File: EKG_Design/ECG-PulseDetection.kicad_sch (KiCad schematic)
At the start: 0 parts

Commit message: Started EKG-Details and ECG-PulseDetection Circuit Symbols implemented
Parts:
- added C11: C_Small, symbol Device:C_Small
- added D1, D2: BAR43FILM, Package_TO_SOT_SMD:SOT-23, symbol Diode:BAR43FILM
- added D3: LED, symbol Device:LED
- added Q1: BC848, Package_TO_SOT_SMD:SOT-23, symbol Transistor_BJT:BC848
- added R3, R4: R, symbol Device:R
- added RV1, RV2: R_Potentiometer, symbol Device:R_Potentiometer
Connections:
- new net: D3.2 (A), R4.2
- new net: C11.1, D2.3 (K), R3.1, RV2.2, RV2.3
- new net: D1.3 (K), D2.1 (A), RV1.2
- new net: Q1.1 (B), R3.2
- new net: D3.1 (K), Q1.3 (C)
- new net 5V0_Analog: R4.1
- new net ECG_Out: RV1.1
- new net GNDD: C11.2, Q1.2 (E), RV1.3, RV2.1
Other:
- company: (none) -> HAWK
- title: (none) -> EKG-Verstärker

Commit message: Finished EKG Schematic
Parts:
- removed D1, D2: BAR43FILM, Package_TO_SOT_SMD:SOT-23, symbol Diode:BAR43FILM
- added D103: BAR43SFILM, Package_TO_SOT_SMD:SOT-23, symbol CustomSymbols:BAR43SFILM
- C301: renamed from C11; value C_Small -> 10u/6.3V X5R
- D303: renamed from D3; value LED -> LED Blau / 0603 / 5mA
- Q301: renamed from Q1; value BC848 -> BC848C
- R301: renamed from R3; value R -> 1k00 1%; symbol Device:R -> Custom_Device:R
- R302: renamed from R4; value R -> 1k00 1%
- RV301: renamed from RV1; value R_Potentiometer -> 1k / 25%
- RV302: renamed from RV2; value R_Potentiometer -> 1k /25%
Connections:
- net at C301.1, RV302.2, RV302.3: now also R301.2, D103.3 (K); no longer R301.1
- net at RV301.2: now also D103.1 (A)
- net at Q301.1 (B): now also R301.1; no longer R301.2
- net GNDD renamed GND
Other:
- moved on the sheet: R301

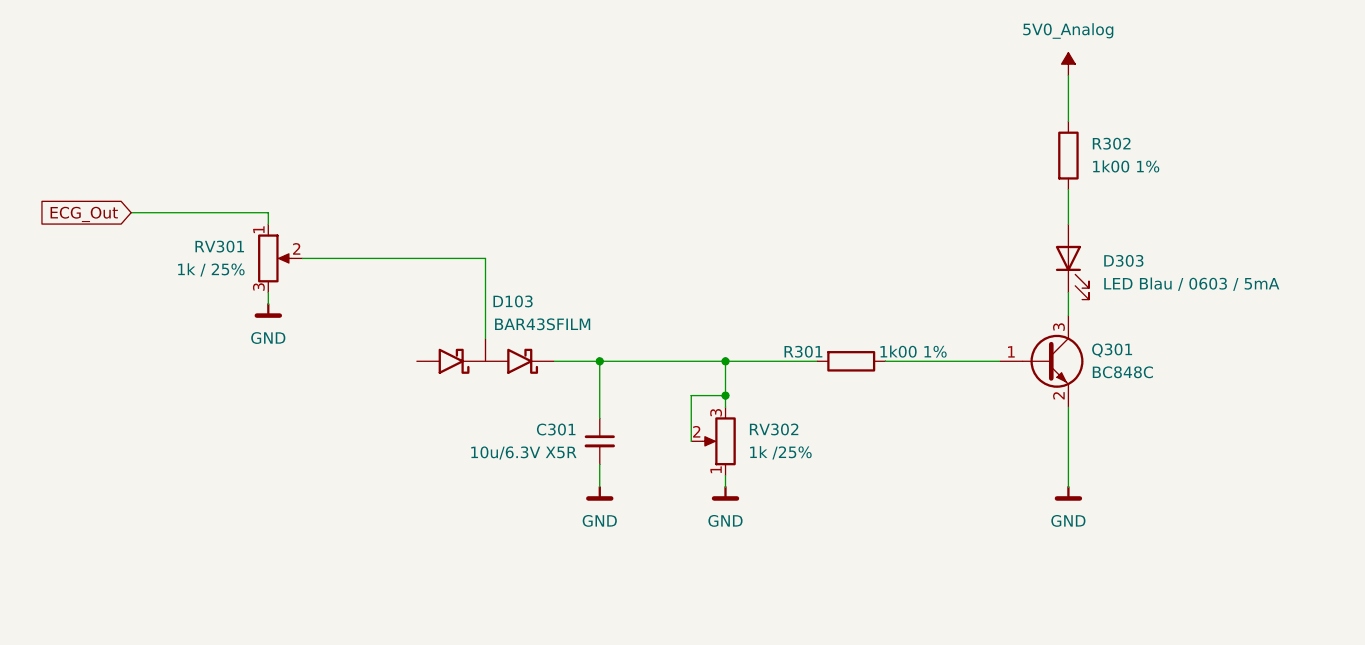
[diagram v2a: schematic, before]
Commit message: Finished ECG Schematic and finished laying out the PCB
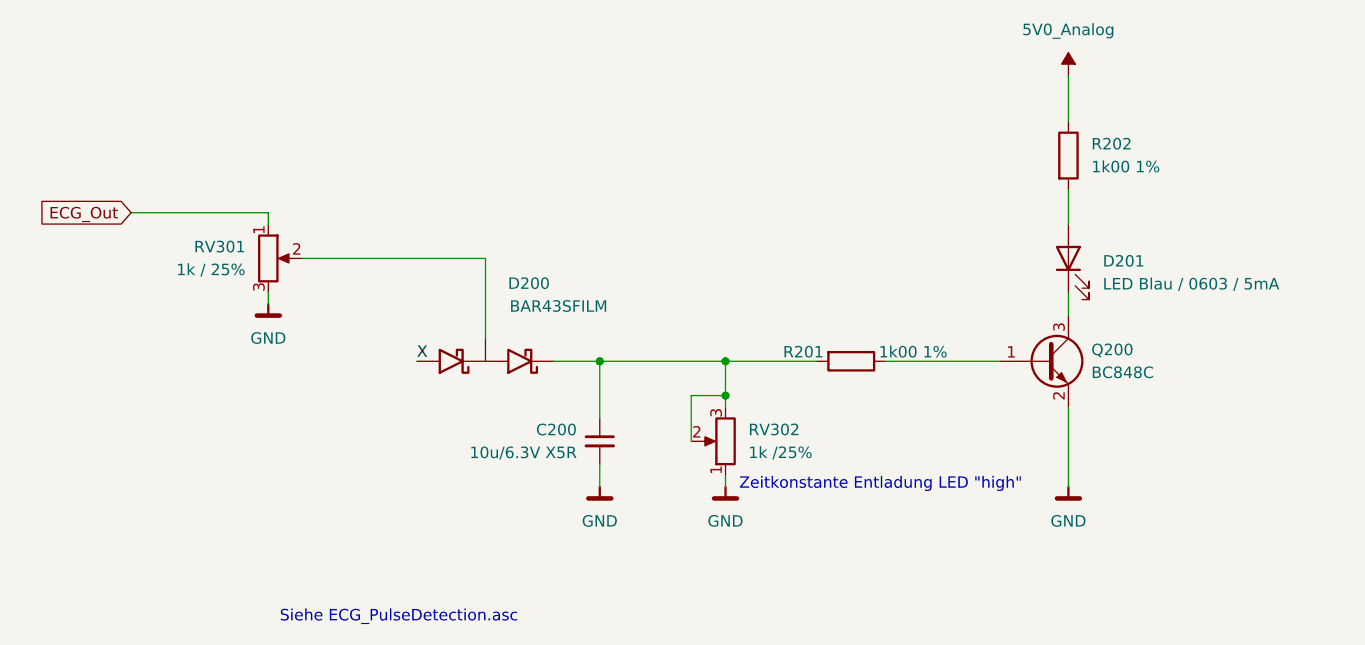
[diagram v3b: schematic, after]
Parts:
- C200: renamed from C301; footprint (none) -> Capacitor_SMD:C_0603_1608Metric_Pad1.08x0.95mm_HandSolder
- D201: renamed from D303; footprint (none) -> LED_SMD:LED_0603_1608Metric_Pad1.05x0.95mm_HandSolder
- R201: renamed from R301; footprint (none) -> Resistor_SMD:R_0603_1608Metric_Pad0.98x0.95mm_HandSolder
- R202: renamed from R302; footprint (none) -> Resistor_SMD:R_0603_1608Metric_Pad0.98x0.95mm_HandSolder
- RV301, RV302: footprint (none) -> Potentiometer_SMD:Potentiometer_Bourns_TC33X_Vertical
- renumbered D103 to D200, Q301 to Q200
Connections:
- net at RV301.2: now also D200.2 (B); no longer D200.1 (A)
- net X: now reaches D200.1 (A)
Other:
- note added: "Siehe ECG_PulseDetection.asc"
- note added: "Zeitkonstante Entladung LED "high""
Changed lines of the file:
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@@
 		(comment 3 "T. Brown")
+	)
+	(text "Zeitkonstante Entladung LED \"high\""
+		(exclude_from_sim no)
+		(at 152.654 111.506 0)
+		(effects
+			(font
+				(size 1.27 1.27)
+			)
+			(justify left)
+		)
+	)
+	(text "Siehe ECG_PulseDetection.asc\n"
+		(exclude_from_sim no)
+		(at 101.6 126.238 0)
+		(effects
+			(font
+				(size 1.27 1.27)
+			)
+			(justify left)
+		)
 	)
 	(junction
@@
 			(width 0)
 			(type default)
+		)
+	)
+	(label "X"
+		(at 116.84 97.79 0)
+		(effects
+			(font
+				(size 1.27 1.27)
+			)
+			(justify left bottom)
 		)
 	)
@@
 		(dnp no)
 		(fields_autoplaced yes)
-		(property "Reference" "R302"
+		(property "Reference" "R202"
 			(at 191.77 73.6599 0)
 			(show_name no)
@@
 			)
 		)
-		(property "Footprint" ""
+		(property "Footprint" "Resistor_SMD:R_0603_1608Metric_Pad0.98x0.95mm_HandSolder"
 			(at 187.452 74.93 90)
 			(hide yes)
@@
 			(project "EKG_Design"
 				(path "/145a8612-0e2a-4b7d-8919-051e741c5f83/fe64ce13-db8d-4cbc-a2e1-b13f0e1fcfb5"
-					(reference "R302")
+					(reference "R202")
 					(unit 1)
 				)
@@
 			)
 		)
-		(property "Footprint" ""
+		(property "Footprint" "Potentiometer_SMD:Potentiometer_Bourns_TC33X_Vertical"
 			(at 151.13 106.68 0)
 			(hide yes)
@@
 		(in_pos_files yes)
 		(dnp no)
-		(property "Reference" "C301"
+		(property "Reference" "C200"
 			(at 134.62 105.4162 0)
 			(show_name no)
@@
 			)
 		)
-		(property "Footprint" ""
+		(property "Footprint" "Capacitor_SMD:C_0603_1608Metric_Pad1.08x0.95mm_HandSolder"
 			(at 137.16 106.68 0)
 			(hide yes)
@@
 			(project "EKG_Design"
 				(path "/145a8612-0e2a-4b7d-8919-051e741c5f83/fe64ce13-db8d-4cbc-a2e1-b13f0e1fcfb5"
-					(reference "C301")
+					(reference "C200")
 					(unit 1)
 				)
@@
 		(dnp no)
 		(fields_autoplaced yes)
-		(property "Reference" "R301"
+		(property "Reference" "R201"
 			(at 162.052 96.774 90)
 			(show_name no)
@@
 			)
 		)
-		(property "Footprint" ""
+		(property "Footprint" "Resistor_SMD:R_0603_1608Metric_Pad0.98x0.95mm_HandSolder"
 			(at 165.1 96.012 90)
 			(hide yes)
@@
 			(project "EKG_Design"
 				(path "/145a8612-0e2a-4b7d-8919-051e741c5f83/fe64ce13-db8d-4cbc-a2e1-b13f0e1fcfb5"
-					(reference "R301")
+					(reference "R201")
 					(unit 1)
 				)
@@
 			)
 		)
-		(property "Footprint" ""
+		(property "Footprint" "Potentiometer_SMD:Potentiometer_Bourns_TC33X_Vertical"
 			(at 100.33 86.36 0)
 			(hide yes)
@@
 		(dnp no)
 		(fields_autoplaced yes)
-		(property "Reference" "D303"
+		(property "Reference" "D201"
 			(at 193.04 86.6774 90)
 			(show_name no)
@@
 			)
 		)
-		(property "Footprint" ""
+		(property "Footprint" "LED_SMD:LED_0603_1608Metric_Pad1.05x0.95mm_HandSolder"
 			(at 189.23 86.36 0)
 			(hide yes)
@@
 			(project "EKG_Design"
 				(path "/145a8612-0e2a-4b7d-8919-051e741c5f83/fe64ce13-db8d-4cbc-a2e1-b13f0e1fcfb5"
-					(reference "D303")
+					(reference "D201")
 					(unit 1)
 				)
@@
 		(in_pos_files yes)
 		(dnp no)
-		(property "Reference" "D103"
-			(at 127.508 91.186 0)
+		(property "Reference" "D200"
+			(at 129.286 89.154 0)
 			(show_name no)
 			(do_not_autoplace no)
@@
 		)
 		(property "Value" "BAR43SFILM"
-			(at 130.81 93.726 0)
+			(at 132.588 91.694 0)
 			(show_name no)
 			(do_not_autoplace no)
@@
 		)
 		(pin "3"
-		)
-		(pin "1"
 		)
 		(instances
 			(project "EKG_Design"
 				(path "/145a8612-0e2a-4b7d-8919-051e741c5f83/fe64ce13-db8d-4cbc-a2e1-b13f0e1fcfb5"
-					(reference "D103")
+					(reference "D200")
 					(unit 1)
 				)
@@
 		(dnp no)
 		(fields_autoplaced yes)
-		(property "Reference" "Q301"
+		(property "Reference" "Q200"
 			(at 191.77 96.5199 0)
 			(show_name no)
@@
 			(project "EKG_Design"
 				(path "/145a8612-0e2a-4b7d-8919-051e741c5f83/fe64ce13-db8d-4cbc-a2e1-b13f0e1fcfb5"
-					(reference "Q301")
+					(reference "Q200")
 					(unit 1)
 				)

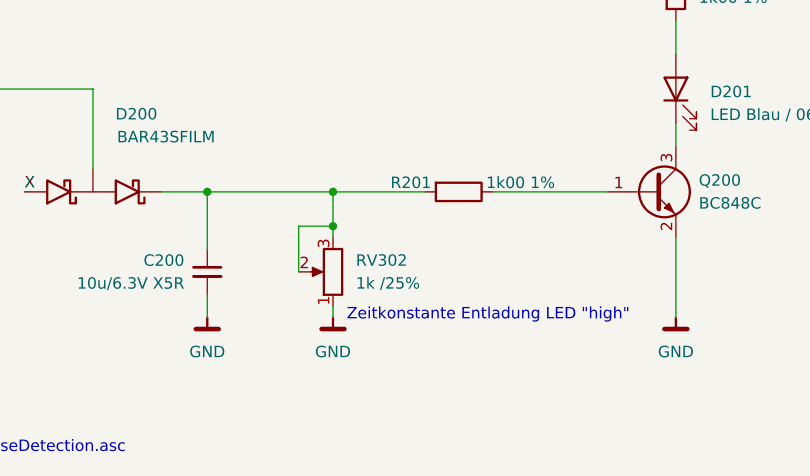
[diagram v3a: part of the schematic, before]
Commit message: adjusted board properties and added manifest items
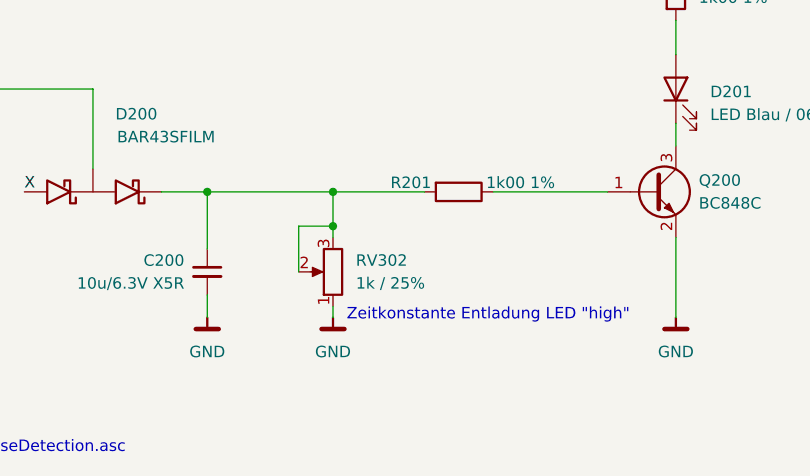
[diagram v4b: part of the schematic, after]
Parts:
- C200: manf# (none) -> CL10A106KQ8NNNC
- D200: manf# (none) -> BAR43SFILM
- D201: manf# (none) -> LB Q39E-L2OO-35-1
- Q200: manf# (none) -> BC848C
- R201, R202: manf# (none) -> RK73H1JTTDD1001F
- RV301: manf# (none) -> TC33X-2-102G
- RV302: value 1k /25% -> 1k / 25%; manf# (none) -> TC33X-2-102G
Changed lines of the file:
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@@
+			)
+		)
+		(property "manf#" "RK73H1JTTDD1001F"
+			(at 189.23 74.93 0)
+			(hide yes)
+			(show_name no)
+			(do_not_autoplace no)
+			(effects
+				(font
+					(size 1.27 1.27)
+				)
 			)
 		)
@@
 			)
 		)
-		(property "Value" "1k /25%"
+		(property "Value" "1k / 25%"
 			(at 153.67 107.9499 0)
 			(show_name no)
@@
 		)
 		(property "Sim.Pins" "1=r0 2=wiper 3=r1"
+			(at 151.13 106.68 0)
+			(hide yes)
+			(show_name no)
+			(do_not_autoplace no)
+			(effects
+				(font
+					(size 1.27 1.27)
+				)
+			)
+		)
+		(property "manf#" "TC33X-2-102G"
 			(at 151.13 106.68 0)
 			(hide yes)
@@
 			)
 		)
+		(property "manf#" "CL10A106KQ8NNNC"
+			(at 137.16 106.68 0)
+			(hide yes)
+			(show_name no)
+			(do_not_autoplace no)
+			(effects
+				(font
+					(size 1.27 1.27)
+				)
+			)
+		)
 		(pin "2"
 		)
@@
 			)
 		)
+		(property "manf#" "RK73H1JTTDD1001F"
+			(at 165.1 97.79 90)
+			(hide yes)
+			(show_name no)
+			(do_not_autoplace no)
+			(effects
+				(font
+					(size 1.27 1.27)
+				)
+			)
+		)
 		(pin "1"
 		)
@@
 			)
 		)
+		(property "manf#" "TC33X-2-102G"
+			(at 100.33 86.36 0)
+			(hide yes)
+			(show_name no)
+			(do_not_autoplace no)
+			(effects
+				(font
+					(size 1.27 1.27)
+				)
+			)
+		)
 		(pin "3"
 		)
@@
 			)
 		)
+		(property "manf#" "LB Q39E-L2OO-35-1"
+			(at 189.23 86.36 90)
+			(hide yes)
+			(show_name no)
+			(do_not_autoplace no)
+			(effects
+				(font
+					(size 1.27 1.27)
+				)
+			)
+		)
 		(pin "1"
 		)
@@
 		(property "Description" "30V 0.1A Small signal Schottky diode, SOT-23"
 			(at 124.206 97.79 0)
+			(hide yes)
+			(show_name no)
+			(do_not_autoplace no)
+			(effects
+				(font
+					(size 1.27 1.27)
+				)
+			)
+		)
+		(property "manf#" "BAR43SFILM"
+			(at 124.46 97.79 0)
 			(hide yes)
 			(show_name no)
@@
 			(at 186.69 97.79 0)
 			(hide yes)
+			(show_name no)
+			(do_not_autoplace no)
+			(effects
+				(font
+					(size 1.27 1.27)
+				)
+			)
+		)
+		(property "manf#" "BC848C"
+			(at 186.69 97.79 0)
+			(hide yes)
